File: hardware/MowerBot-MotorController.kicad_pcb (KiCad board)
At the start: 2 copper layers, 65 x 100 mm, 22 parts, among them J7 12V_XT60, U1A ESP32C3_J1, U1B ESP32C3_J3, U2 MINI560

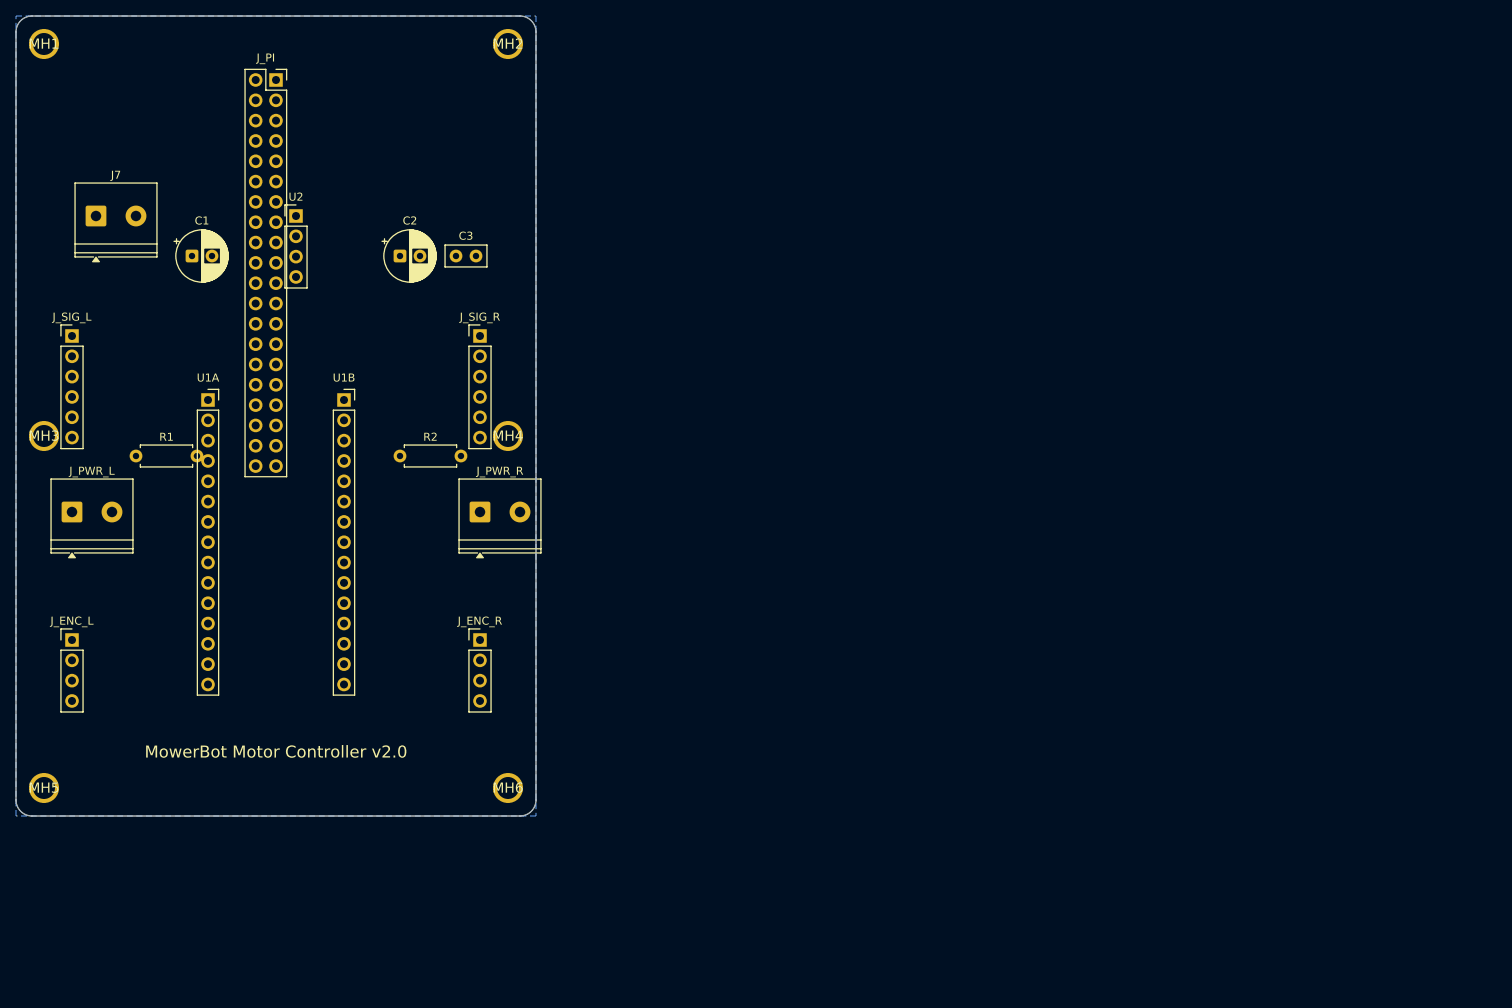
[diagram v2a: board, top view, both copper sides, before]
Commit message: feat(hardware): MowerBot HAT v2.0 motor controller PCB sources
Commit the KiCad project + symbol/footprint libraries + 3D models +
fabrication output for the v2.0 motor controller HAT. Source files
have been live in the working tree since early April but never
committed.

Includes:
- kicad_pcb / kicad_sch / kicad_pro / kicad_prl
- MowerBot.kicad_sym + MowerBot.pretty/ (custom footprints)
- 3D models (ADS1115, BTS7960, GY521 MPU6050, MINI560)
- Schematic PDF + DRC violations report
- production/ (Gerbers, BOM, positions, IPC netlist)
- fabrication-toolkit-options.json
- docs/pcb-motor-controller.md updates
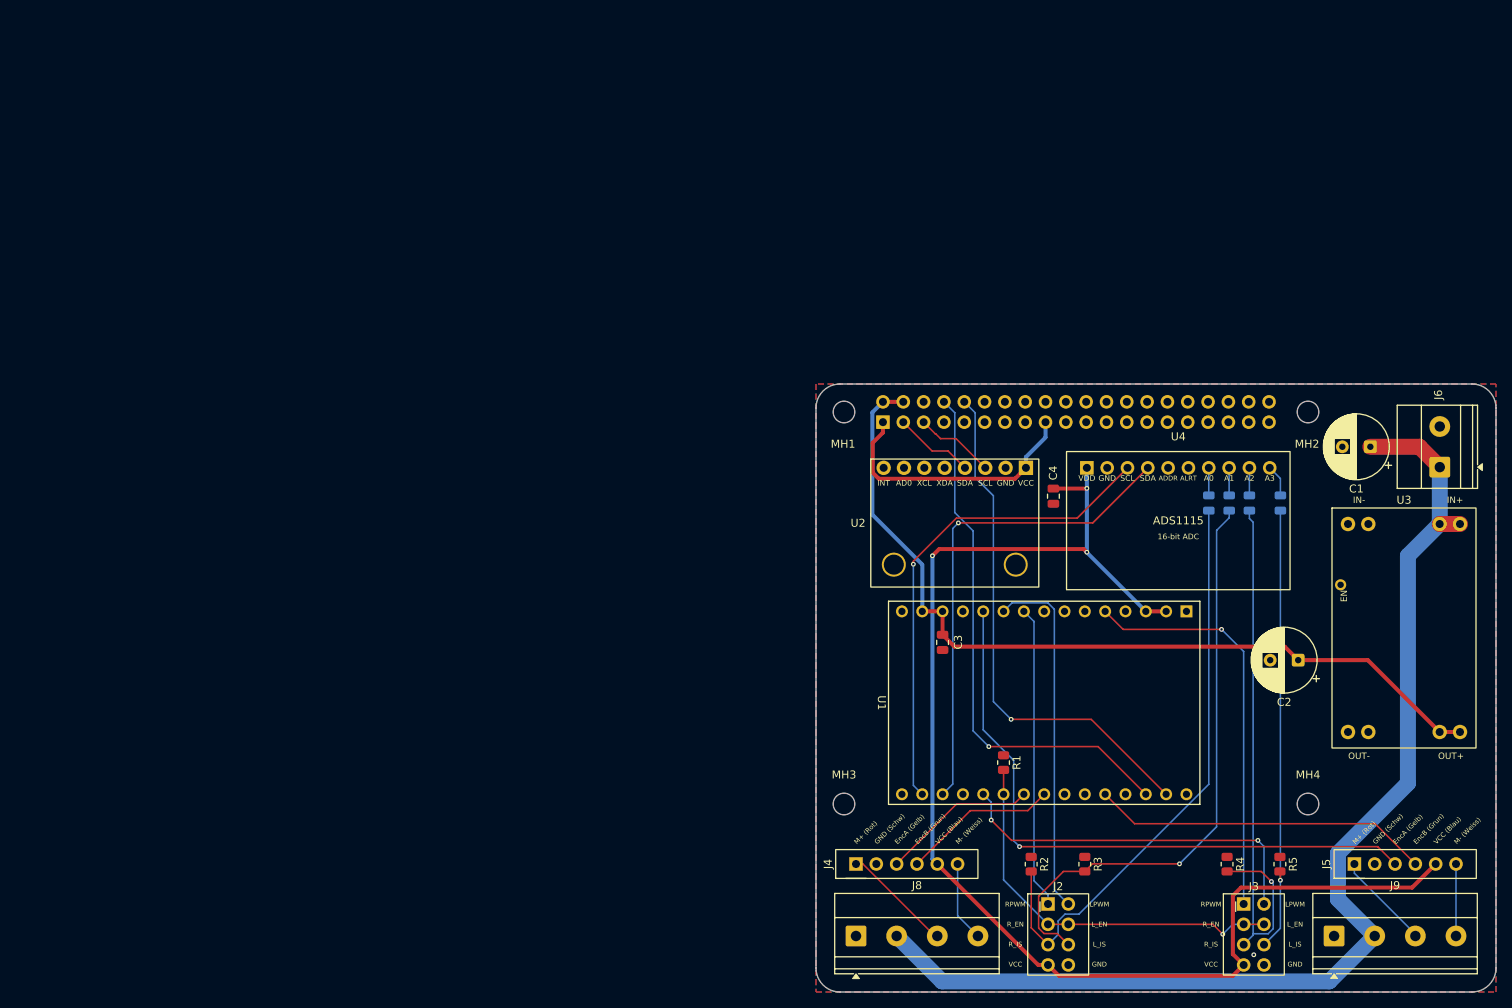
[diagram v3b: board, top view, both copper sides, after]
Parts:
- removed J7: 12V_XT60, TerminalBlock_Phoenix:TerminalBlock_Phoenix_PT-1,5-2-5.0-H_1x02_P5.00mm_Horizontal
- removed J_ENC_L: Encoder_Left, Connector_PinHeader_2.54mm:PinHeader_1x04_P2.54mm_Vertical
- removed J_ENC_R: Encoder_Right, Connector_PinHeader_2.54mm:PinHeader_1x04_P2.54mm_Vertical
- removed J_PI: RPi_GPIO_40Pin, Connector_PinSocket_2.54mm:PinSocket_2x20_P2.54mm_Vertical
- removed J_PWR_L: BTS7960_L_Power, TerminalBlock_Phoenix:TerminalBlock_Phoenix_PT-1,5-2-5.0-H_1x02_P5.00mm_Horizontal
- removed J_PWR_R: BTS7960_R_Power, TerminalBlock_Phoenix:TerminalBlock_Phoenix_PT-1,5-2-5.0-H_1x02_P5.00mm_Horizontal
- removed J_SIG_L: BTS7960_L_Signal, Connector_PinHeader_2.54mm:PinHeader_1x06_P2.54mm_Vertical
- removed J_SIG_R: BTS7960_R_Signal, Connector_PinHeader_2.54mm:PinHeader_1x06_P2.54mm_Vertical
- removed MH5, MH6: MountingHole_2.75mm, 
- removed U1A: ESP32C3_J1, Connector_PinSocket_2.54mm:PinSocket_1x15_P2.54mm_Vertical
- removed U1B: ESP32C3_J3, Connector_PinSocket_2.54mm:PinSocket_1x15_P2.54mm_Vertical
- added C4: 100nF, Capacitor_SMD:C_0805_2012Metric, F.Cu at (129.7, 60.0)
- added C5: 10nF, Capacitor_SMD:C_0805_2012Metric, B.Cu at (149.1, 60.9)
- added C6: 10nF, Capacitor_SMD:C_0805_2012Metric, B.Cu at (151.7, 60.9)
- added C7: 10nF, Capacitor_SMD:C_0805_2012Metric, B.Cu at (154.2, 60.9)
- added C8: 10nF, Capacitor_SMD:C_0805_2012Metric, B.Cu at (158.1, 60.9)
- added J1: Raspberry_Pi_4, Connector_PinSocket_2.54mm:PinSocket_2x20_P2.54mm_Vertical, B.Cu at (108.4, 50.8)
- added J2: BTS7960_Left, MowerBot:BTS7960, F.Cu at (130.3, 114.8)
- added J3: BTS7960_Right, MowerBot:BTS7960, F.Cu at (154.7, 114.8)
- added J4: JGB37_520 Left, MowerBot:JGB37_520, F.Cu at (105.0, 106.0)
- added J5: JGB37_520 Right, MowerBot:JGB37_520, F.Cu at (167.3, 106.0)
- added J6: Screw_Terminal_01x02, TerminalBlock_Phoenix:TerminalBlock_Phoenix_MKDS-1,5-2-5.08_1x02_P5.08mm_Horizontal, F.Cu at (178.0, 56.4)
- added J8: Screw_Terminal_01x04_Left, TerminalBlock_Phoenix:TerminalBlock_Phoenix_MKDS-1,5-4-5.08_1x04_P5.08mm_Horizontal, F.Cu at (105.0, 115.0)
- added J9: Screw_Terminal_01x04_Right, TerminalBlock_Phoenix:TerminalBlock_Phoenix_MKDS-1,5-4-5.08_1x04_P5.08mm_Horizontal, F.Cu at (164.8, 115.0)
- added R3: R, Resistor_SMD:R_0805_2012Metric, F.Cu at (133.6, 106.0)
- added R4: R, Resistor_SMD:R_0805_2012Metric, F.Cu at (151.4, 106.0)
- added R5: R, Resistor_SMD:R_0805_2012Metric, F.Cu at (158.0, 106.0)
- added U1: ESP32-C3-DevKitM-1, RF_Module:ESP32-C3-DevKitM-1, F.Cu at (146.3, 74.4)
- added U3: MINI560, MowerBot:MINI560, F.Cu at (173.5, 76.5)
- added U4: ADS1115, MowerBot:ADS1115, F.Cu at (145.3, 63.1)
- C1: value 100uF/25V -> 100uF/50V; footprint Capacitor_THT:CP_Radial_D6.3mm_P2.50mm -> Capacitor_THT:CP_Radial_D8.0mm_P3.50mm
- C2: value 100uF/16V -> 100uF/50V; footprint Capacitor_THT:CP_Radial_D6.3mm_P2.50mm -> Capacitor_THT:CP_Radial_D8.0mm_P3.50mm
- C3: footprint Capacitor_THT:C_Disc_D5.0mm_W2.5mm_P2.50mm -> Capacitor_SMD:C_0805_2012Metric
- MH1, MH2, MH3, MH4: footprint (none) -> MountingHole:MountingHole_2.7mm_M2.5
- R1, R2: value 10k -> R; footprint Resistor_THT:R_Axial_DIN0207_L6.3mm_D2.5mm_P7.62mm_Horizontal -> Resistor_SMD:R_0805_2012Metric
- U2: value MINI560 -> GY521_MPU6050; footprint Connector_PinHeader_2.54mm:PinHeader_1x04_P2.54mm_Vertical -> MowerBot:GY521_MPU6050
- moved C1 149.2 mm to (169.3, 53.8), turned to 180 degrees
- moved C2 123.1 mm to (160.3, 80.5), turned to 180 degrees
- moved R1 115.0 mm to (123.4, 93.3), turned to -90 degrees
- moved MH1 110.1 mm to (103.5, 49.5)
- moved MH2 110.1 mm to (161.5, 49.5)
- moved MH3 110.1 mm to (103.5, 98.5)
- moved MH4 110.1 mm to (161.5, 98.5)
- moved R2 94.0 mm to (126.9, 106.0), turned to -90 degrees
- moved U2 90.9 mm to (117.3, 63.4)
- moved C3 77.7 mm to (115.8, 78.3), turned to -90 degrees
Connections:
- C1 pad 1: (no net) -> /+12V
- C1 pad 2: (no net) -> /GND
- C2 pad 1: (no net) -> /+5V
- C2 pad 2: (no net) -> /GND
- C3 pad 1: (no net) -> /+5V
- C3 pad 2: (no net) -> /GND
- R1 pad 1: (no net) -> /GND
- R1 pad 2: (no net) -> /MOT_EN
- R2 pad 1: (no net) -> /GND
- R2 pad 2: (no net) -> /ML_R_IS
- U2 pad 1: (no net) -> /+3V3
- U2 pad 2: (no net) -> /GND
- U2 pad 3: (no net) -> /I2C_SCL
- U2 pad 4: (no net) -> /I2C_SDA
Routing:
- net /+3V3: track 0.00 -> 200.8 mm, vias 0 -> 3
- net /+12V: track 0.00 -> 142.5 mm
- net /+5V: track 0.00 -> 107.0 mm
- net /ENC_R_A: track 0.00 -> 79.1 mm, vias 0 -> 1
- net /ML_L_IS: track 0.00 -> 74.6 mm, vias 0 -> 1
- net /ML_R_IS: track 0.00 -> 73.6 mm
- net /MR_R_IS: track 0.00 -> 69.8 mm, vias 0 -> 1
- net /UART_TX_PI: track 0.00 -> 67.5 mm, vias 0 -> 1
- net /UART_RX_PI: track 0.00 -> 65.4 mm, vias 0 -> 1
- net /I2C_ESP_SDA: track 0.00 -> 61.3 mm, vias 0 -> 1
- net /I2C_ESP_SCL: track 0.00 -> 61.2 mm, vias 0 -> 1
- net /MR_L_IS: track 0.00 -> 56.2 mm, vias 0 -> 1
- net /MR_RPWM: track 0.00 -> 51.0 mm, vias 0 -> 1
- net /MOT_EN: track 0.00 -> 49.6 mm, vias 0 -> 1
- net /MR_LPWM: track 0.00 -> 46.3 mm, vias 0 -> 2
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- added copper zone on B.Cu, net /GND
- added copper zone on F.Cu, net /GND
- removed copper zone on B.Cu, net GND
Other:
- board size 65 x 100 mm -> 85 x 76 mm
- board text removed: "MowerBot Motor Controller v2.0"
